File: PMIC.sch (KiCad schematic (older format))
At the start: 60 parts, among them U3 BD71847MWV, Y1 Crystal

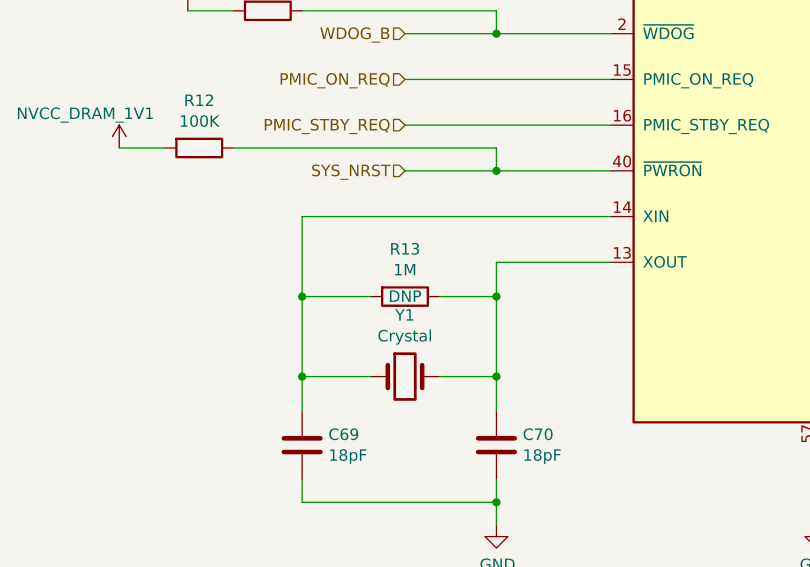
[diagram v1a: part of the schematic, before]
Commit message: Complete entry of bom
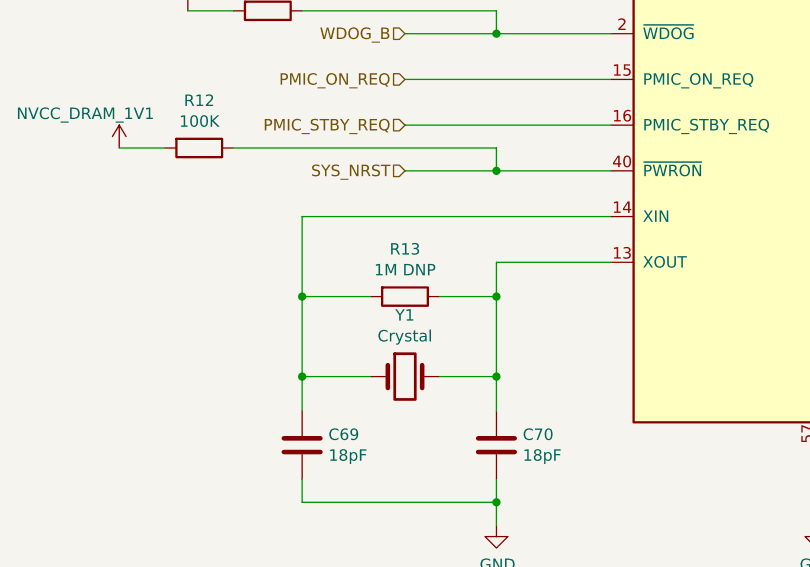
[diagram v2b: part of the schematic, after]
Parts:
- C35, C36, C43, C48, C53, C54, C58, C62: Mfgr (none) -> Samsung; Part (none) -> CL10X106MO8NRNC; Vendorpart (none) -> 1276-6769-1-ND
- C37, C38, C45, C46, C50, C51, C55, C56, C60, C61, C64, C65: Mfgr (none) -> Murata; Part (none) -> GRM188C80G226MEA0D; Vendorpart (none) -> 490-7196-1-ND
- C39, C44, C47, C52, C57, C67, C68: Mfgr (none) -> Murata; Part (none) -> GRM155C81A105KA12D; Vendorpart (none) -> 490-12699-1-ND
- C40, C41, C42: Mfgr (none) -> Murata; Part (none) -> GRM155C80J225ME95D; Vendorpart (none) -> 490-10013-1-ND
- C49, C59, C66: Mfgr (none) -> Murata; Part (none) -> GRM155C80J475MEAAD; Vendorpart (none) -> 490-14458-1-ND
- C63: Mfgr (none) -> Samsung; Part (none) -> CL10B105MO8NNWC; Vendorpart (none) -> 1276-6524-1-ND
- C69, C70: Mfgr (none) -> Murata; Part (none) -> GRM0335C1H180JA01D; Vendorpart (none) -> 490-6117-1-ND
- L1, L2, L3, L5, L6: Mfgr (none) -> Samsung; Part (none) -> CIGT201610EHR47MNE; Vendorpart 240-3079-1-ND -> 1276-6902-1-ND
- L4: Mfgr (none) -> Samsung; Part (none) -> CIGT201610EH1R0MNE; Vendorpart 240-3079-1-ND -> 1276-6900-1-ND
- R11, R12: Mfgr (none) -> Yageo; Part (none) -> RC0402JR-07100KL; Vendorpart (none) -> 311-100KJRCT-ND
- R13: value 1M -> 1M DNP; Part DNP -> (none)
- U3: Mfgr (none) -> ROHM; Part (none) -> BD71847AMWV-E2; Vendorpart (none) -> BD71847AMWV-E2CT-ND
- Y1: Mfgr (none) -> Abracon; Part (none) -> ABS07-32.768KHZ-T

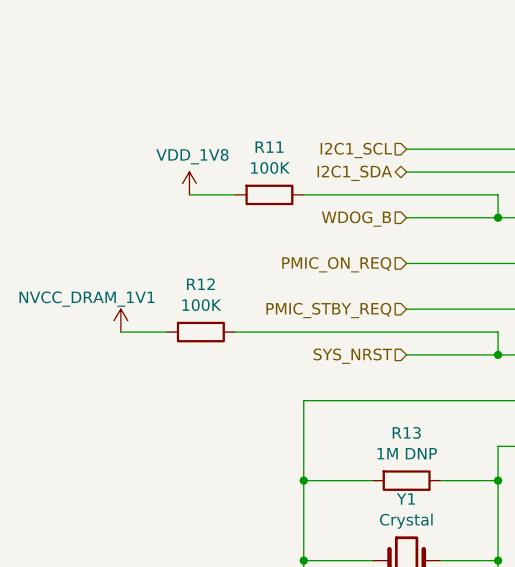
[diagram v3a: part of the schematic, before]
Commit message: Set up for battery NTC and add a power button
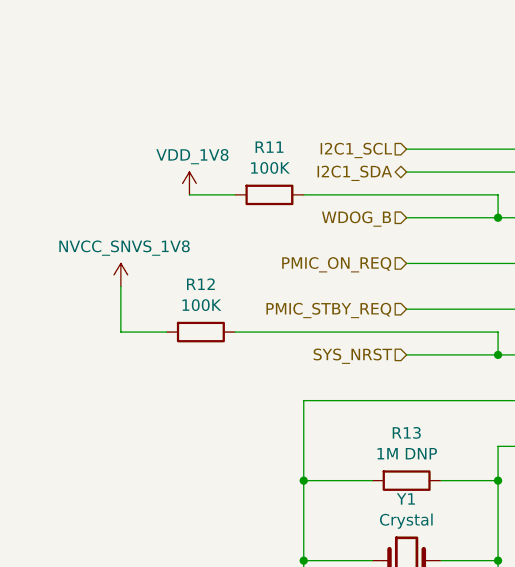
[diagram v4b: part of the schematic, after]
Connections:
- net NVCC_DRAM_1V1: no longer R12.2
- net NVCC_SNVS_1V8: now also R12.2
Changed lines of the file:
@@
 EESchema Schematic File Version 4
-LIBS:mxenc-cache
-EELAYER 29 0
+EELAYER 30 0
 EELAYER END
 $Descr B 17000 11000
 encoding utf-8
 Sheet 4 10
-Title ""
-Date ""
-Rev ""
-Comp ""
+Title "kimχ micro"
+Date "2020-03-05"
+Rev "0.9"
+Comp "GroupGets"
 Comment1 ""
 Comment2 ""
@@
 SYS_NRST
 $Comp
-L mxenc:NVCC_DRAM_1V1 #PWR043
-U 1 1 5D9DBDA9
-P 2550 7150
-F 0 "#PWR043" H 2550 7000 50  0001 C CNN
-F 1 "NVCC_DRAM_1V1" H 2100 7300 50  0000 L CNN
-F 2 "" H 2550 7150 50  0001 C CNN
-F 3 "" H 2550 7150 50  0001 C CNN
-	1    2550 7150
-	1    0    0    -1
-$EndComp
-$Comp
 L mxenc:VDD_1V8 #PWR042
 U 1 1 5D9DD486
@@
 Wire Wire Line
 	6850 2150 7300 2150
+$Comp
+L mxenc:NVCC_SNVS_1V8 #PWR0277
+U 1 1 5E6C9EEF
+P 2550 6950
+F 0 "#PWR0277" H 2550 6800 50  0001 C CNN
+F 1 "NVCC_SNVS_1V8" H 2565 7123 50  0000 C CNN
+F 2 "" H 2550 6950 50  0001 C CNN
+F 3 "" H 2550 6950 50  0001 C CNN
+	1    2550 6950
+	1    0    0    -1
+$EndComp
+Wire Wire Line
+	2550 6950 2550 7150
 $EndSCHEMATC

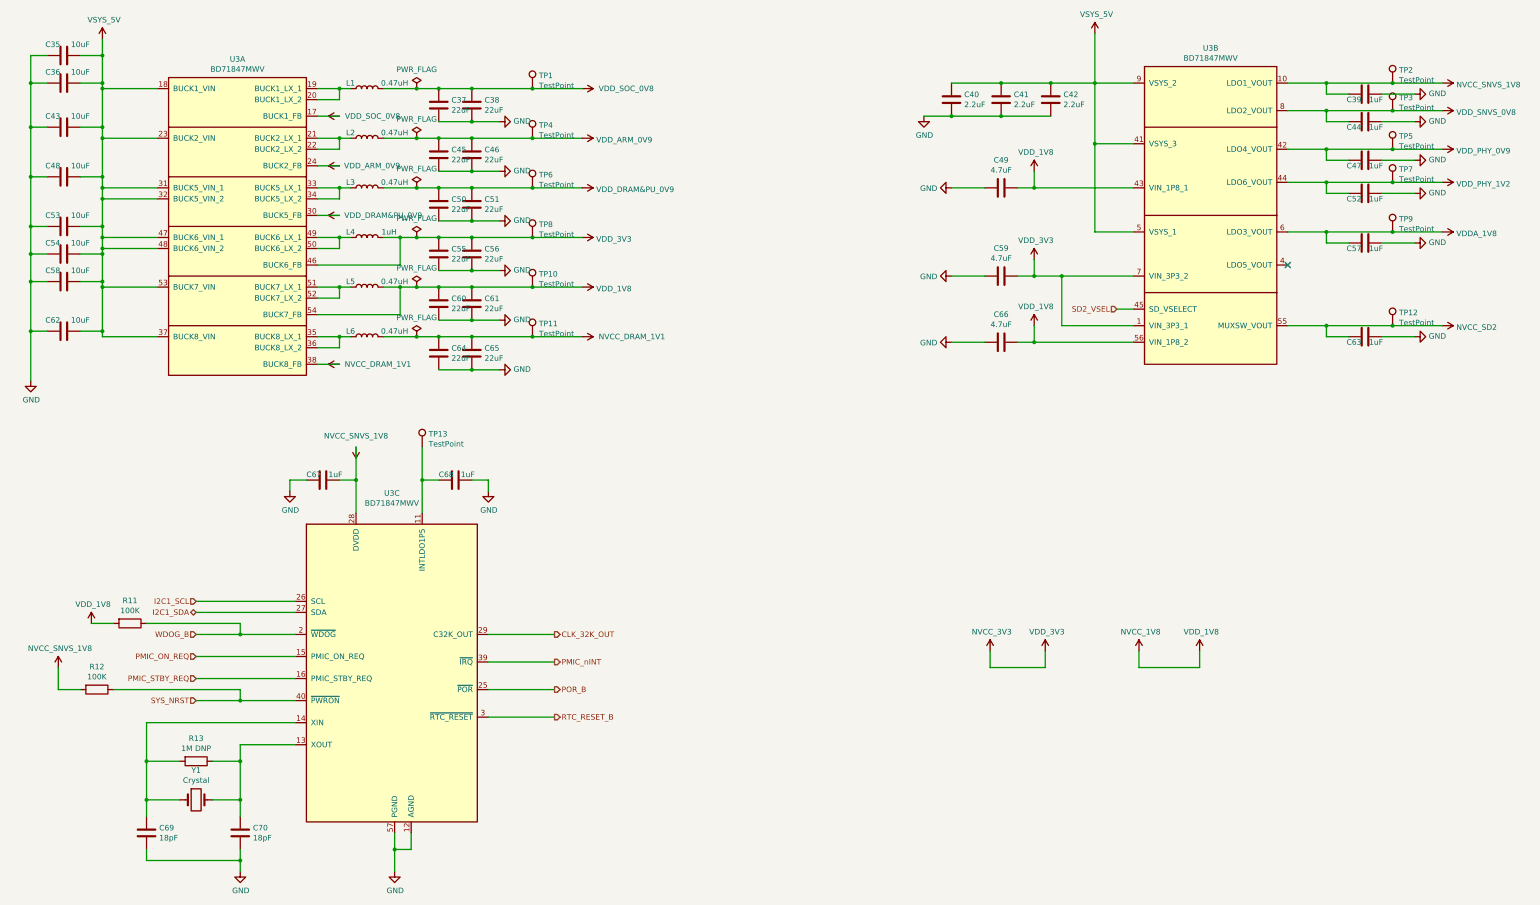
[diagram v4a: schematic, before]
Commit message: Re-annotate schematics, add dnp field, and silkscreen cleanup
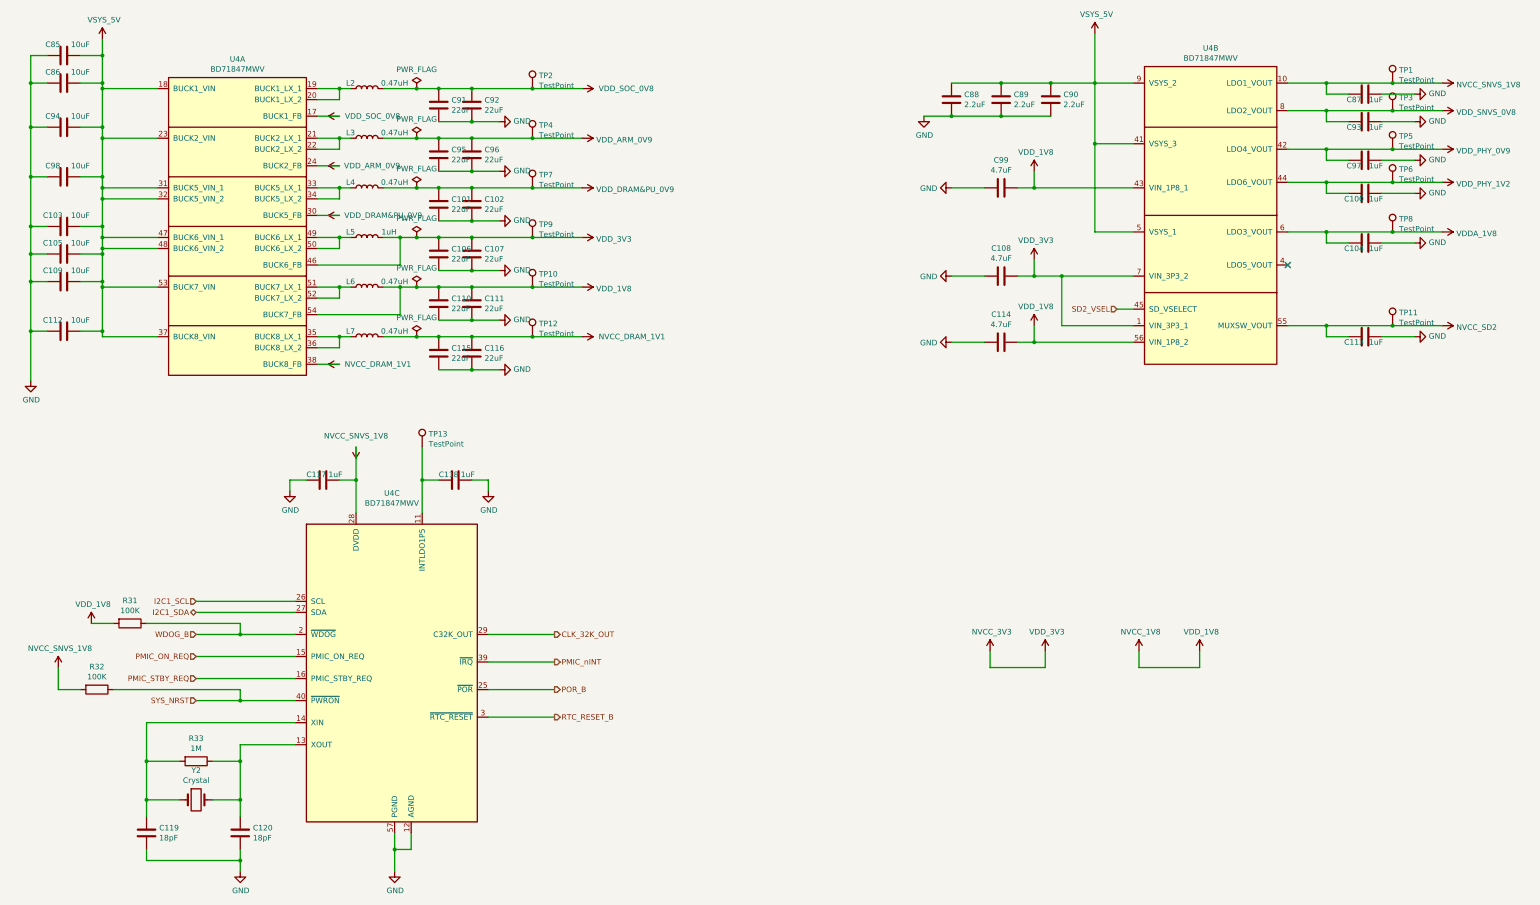
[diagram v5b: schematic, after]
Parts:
- R33: renamed from R13; value 1M DNP -> 1M; Populate (none) -> DNP
- renumbered C52 to C100, C50 to C101, C51 to C102, C53 to C103, C57 to C104, C54 to C105, C55 to C106, C56 to C107, C59 to C108, C58 to C109, C60 to C110, C61 to C111, C62 to C112, C63 to C113, C66 to C114, C64 to C115, C65 to C116, C67 to C117, C68 to C118, C69 to C119, C70 to C120, C35 to C85, C36 to C86, C39 to C87, C40 to C88, C41 to C89, C42 to C90, C37 to C91, C38 to C92, C44 to C93, C43 to C94, C45 to C95, C46 to C96, C47 to C97, C48 to C98, C49 to C99, L1 to L2, L2 to L3, L3 to L4, L4 to L5, L5 to L6, L6 to L7, R11 to R31, R12 to R32, TP2 to TP1, TP12 to TP11, TP11 to TP12, TP1 to TP2, TP7 to TP6, TP6 to TP7, TP9 to TP8, TP8 to TP9, U3 to U4, Y1 to Y2

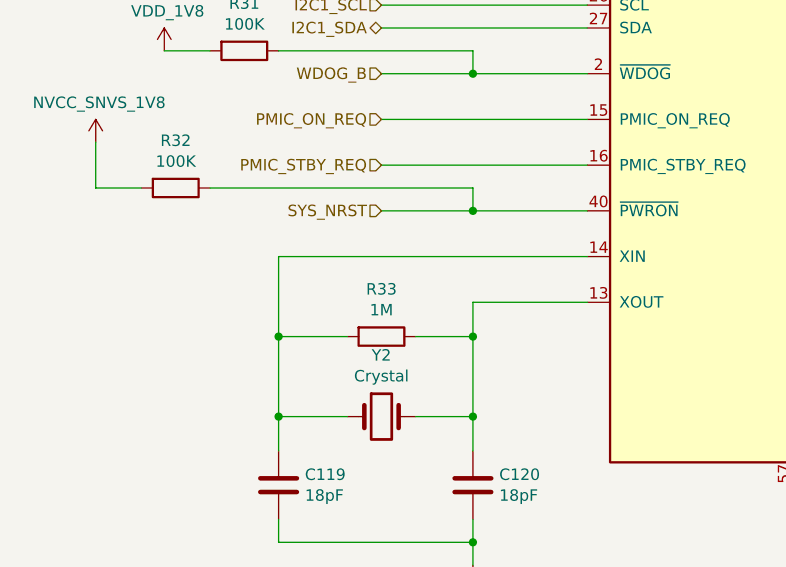
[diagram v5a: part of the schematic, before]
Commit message: Fixed a few comments related to component reference and make sure we're displaying dnp
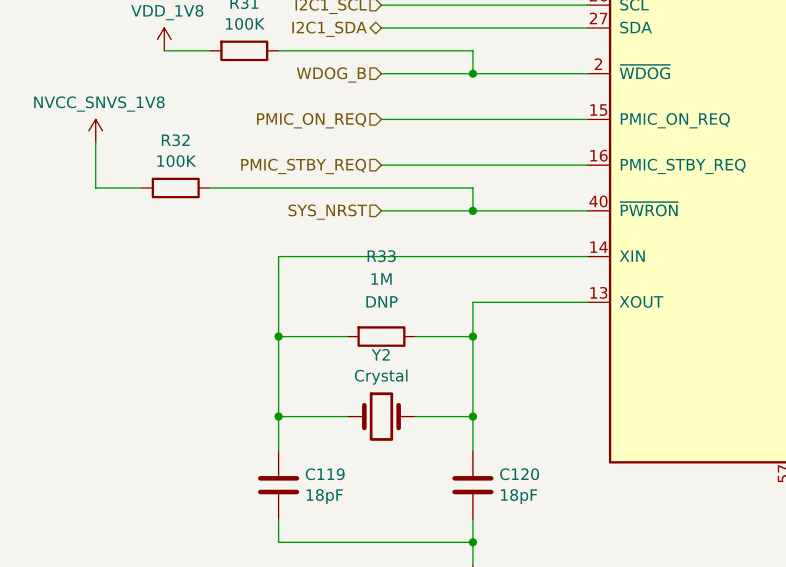
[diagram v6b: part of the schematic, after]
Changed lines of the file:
@@
 U 1 1 5DAA7375
 P 3800 7800
-F 0 "R33" V 3593 7800 50  0000 C CNN
-F 1 "1M" V 3684 7800 50  0000 C CNN
+F 0 "R33" V 3450 7800 50  0000 C CNN
+F 1 "1M" V 3550 7800 50  0000 C CNN
 F 2 "Resistor_SMD:R_0402_1005Metric" V 3730 7800 50  0001 C CNN
 F 3 "~" H 3800 7800 50  0001 C CNN
-F 4 "DNP" H 3800 7800 50  0001 C CNN "Populate"
+F 4 "DNP" V 3650 7800 50  0000 C CNN "Populate"
 	1    3800 7800
 	0    1    1    0
